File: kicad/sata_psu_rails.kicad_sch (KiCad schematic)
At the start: 4 parts

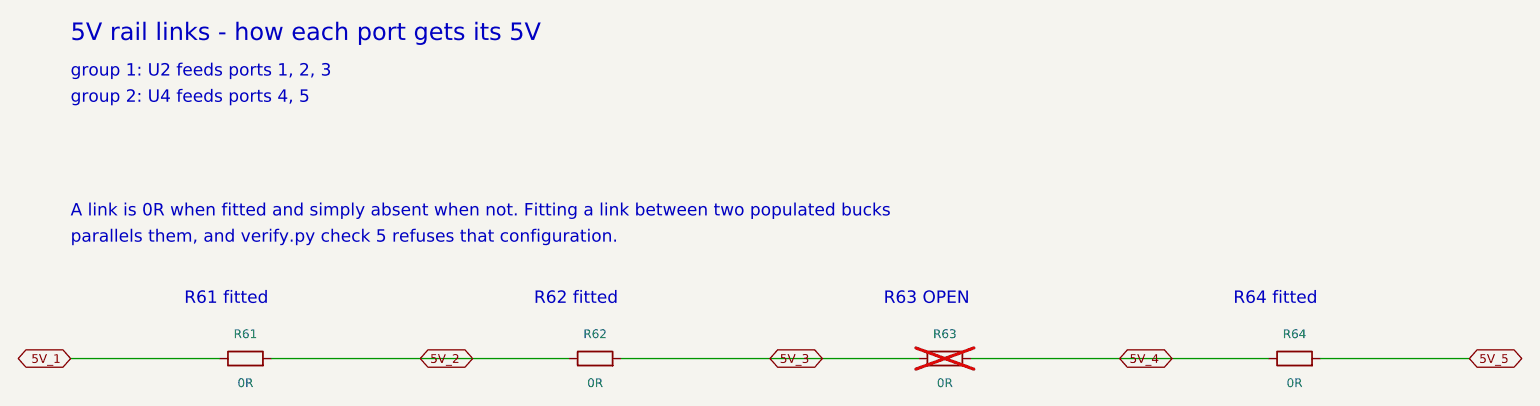
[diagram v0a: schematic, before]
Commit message: v3: JLCPCB-ready layout, fab outputs and DigiKey BOM
Board (DRC clean against JLCPCB standard 2-layer rules, 0 errors,
0 unconnected, schematic parity clean):
- design rules set to JLCPCB limits; extra pad rules in sata_psu.kicad_dru
- buck GND pins (U1-U5) were on isolated F.Cu islands: stitched to B.Cu
- C41/C51 1206 pads restored from 0603 pitch to library land pattern
- replicated SW via patches re-netted (ch2/4/5), missing ones added
- duplicate 12V zone and dangling vias on ch1 removed; 0.4 vias -> 0.45
- gate-cap courtyards in ch4/ch5 cleared; DNP flags synced from schematic
- refdes resized to 1.0/0.15 mm and placed clear of pads and silk

Outputs: Gerbers + Excellon drill (gerbers/, sata_psu_jlcpcb.zip) and
DigiKey BOM with in-stock substitutes plus a cart upload CSV.

Co-Authored-By: Claude Opus 5.5 <noreply@anthropic.com>
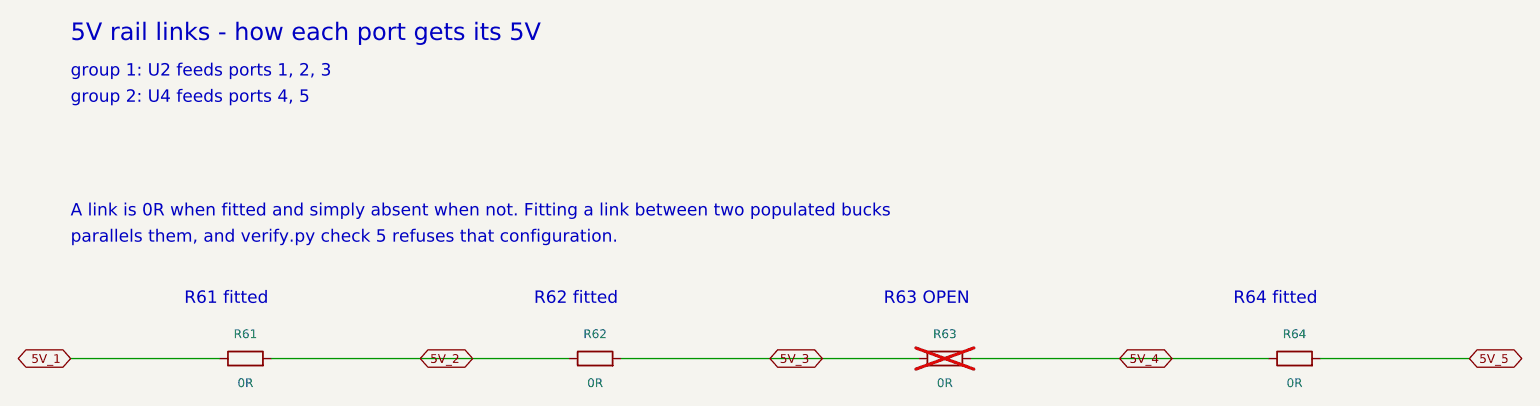
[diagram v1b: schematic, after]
